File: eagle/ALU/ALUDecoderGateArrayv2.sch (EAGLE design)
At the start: 0 parts

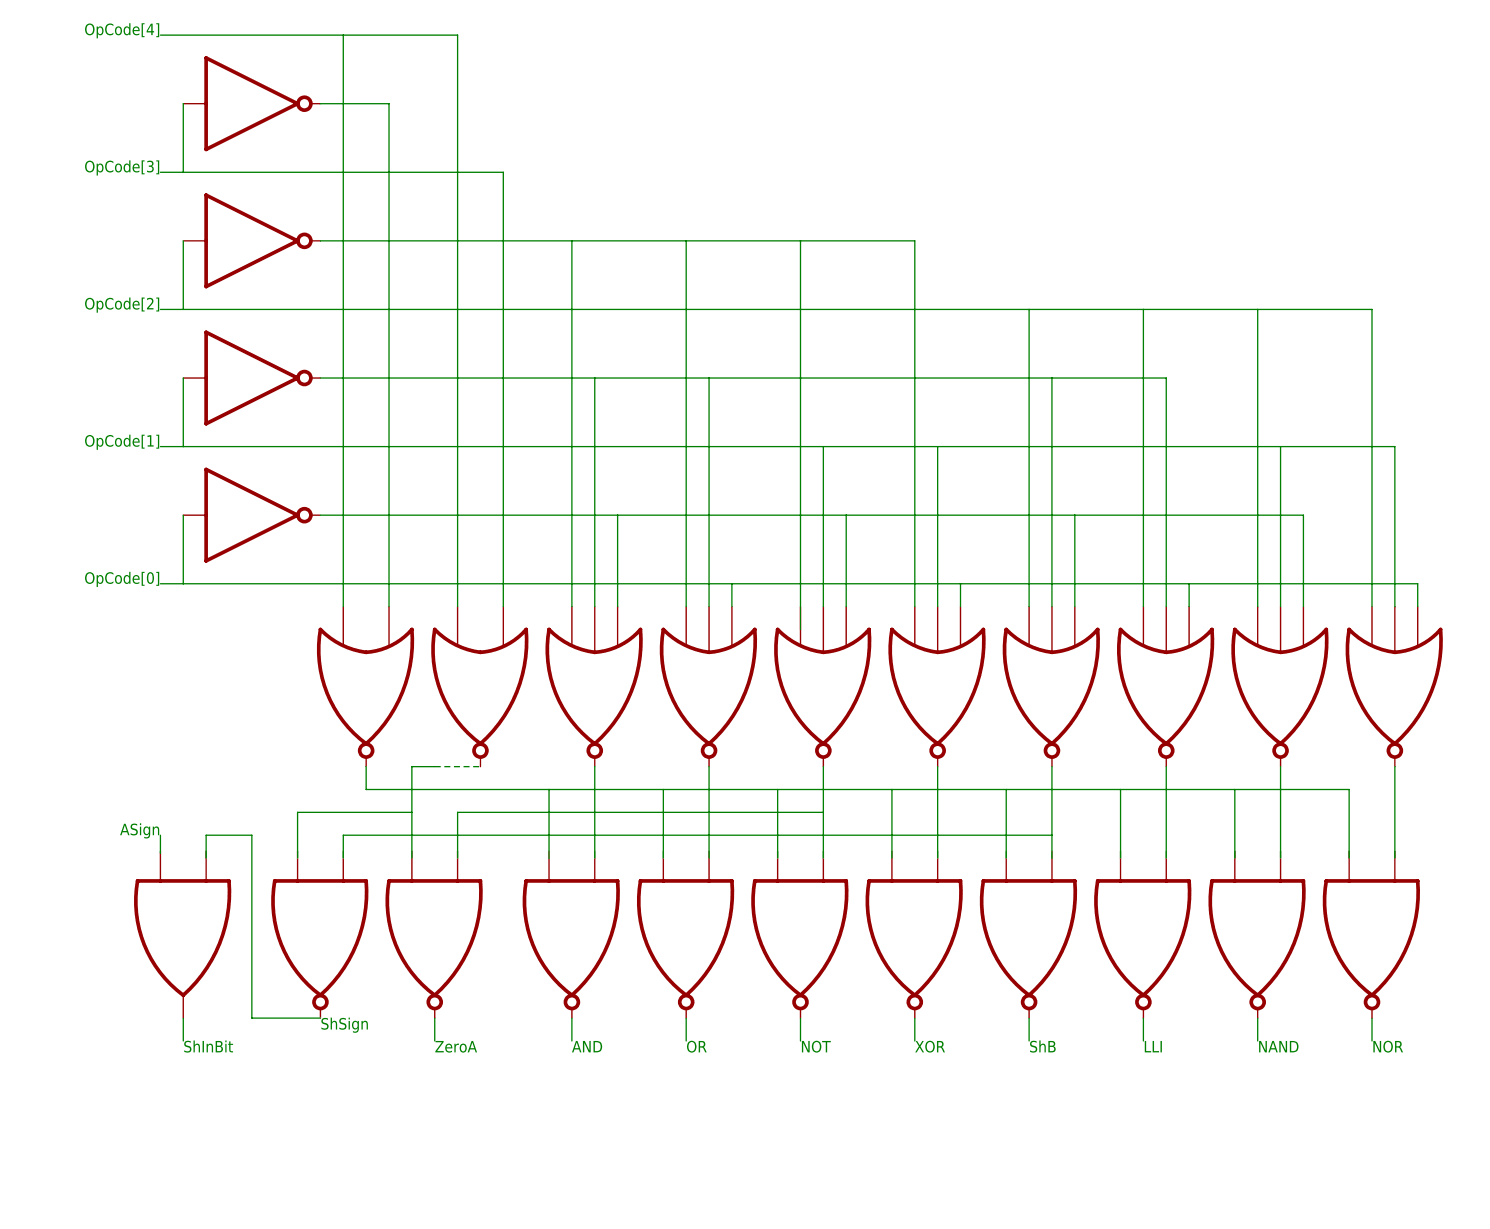
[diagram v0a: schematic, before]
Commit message: Eagle schematics now use library
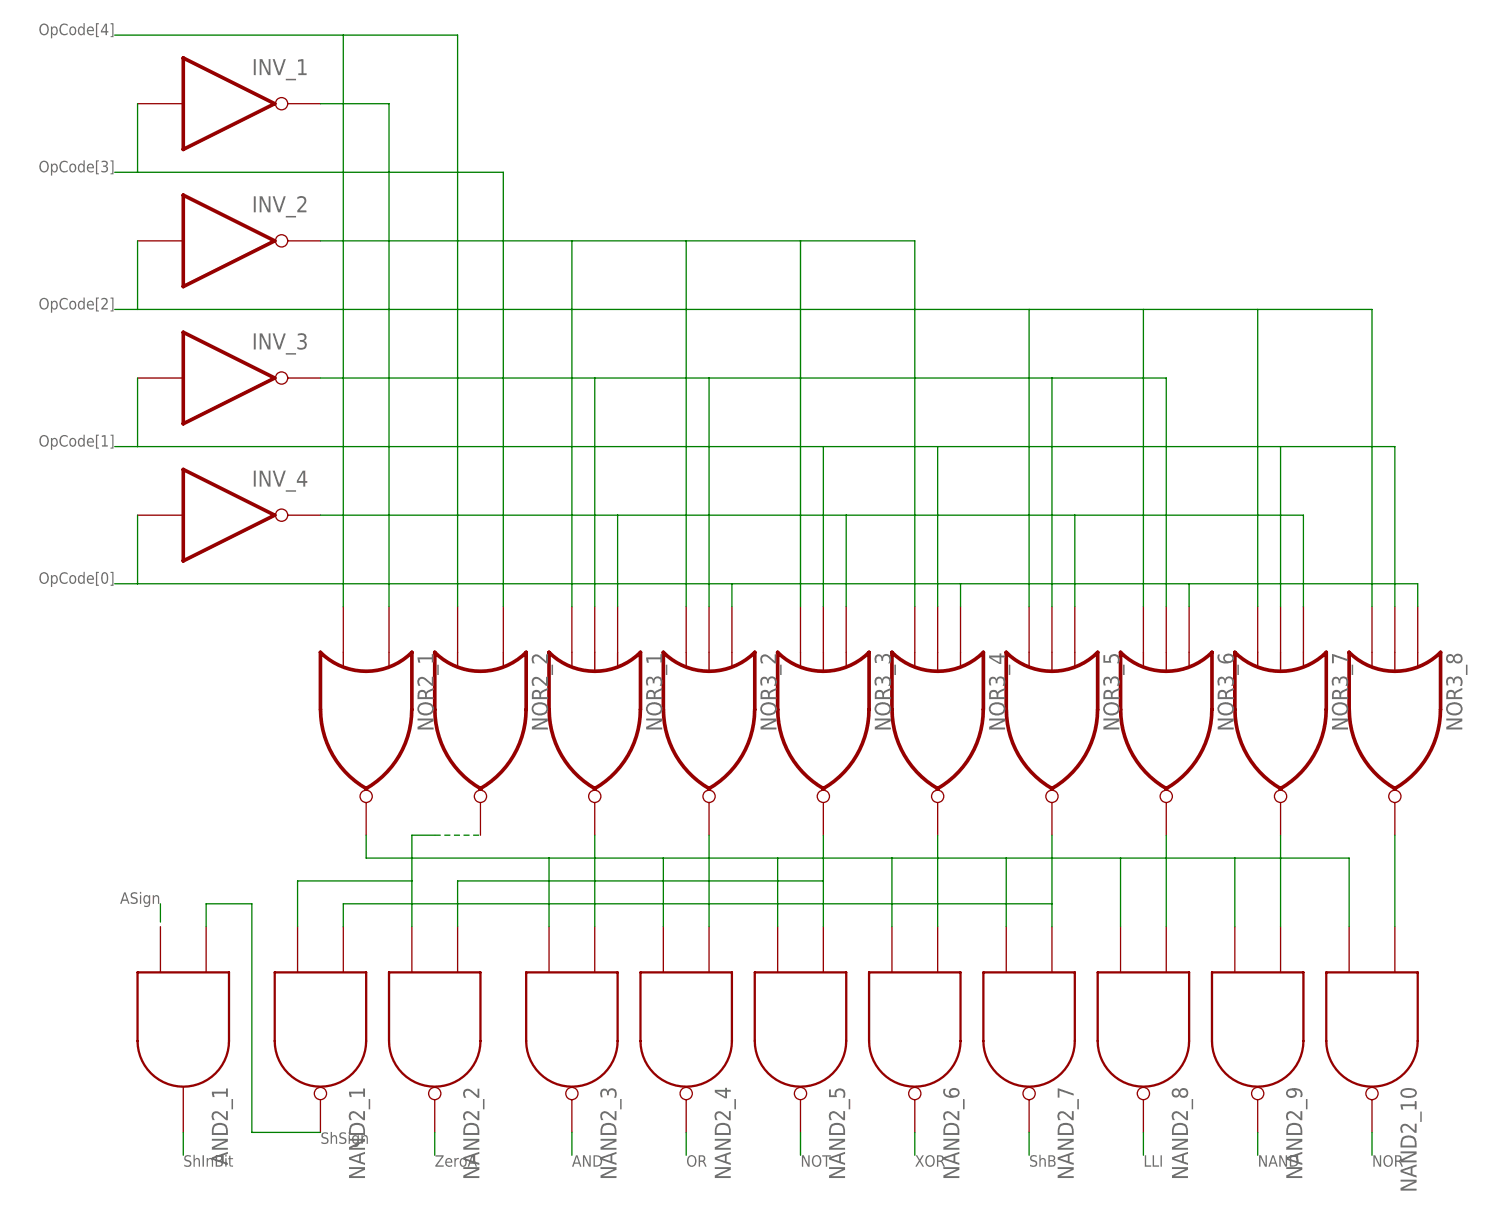
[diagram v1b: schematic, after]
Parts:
- added AND2_1: AND2, c035u:AND2
- added INV_1, INV_2, INV_3, INV_4: INV, c035u:INV
- added NAND2_1, NAND2_10, NAND2_2, NAND2_3, NAND2_4, NAND2_5, NAND2_6, NAND2_7, NAND2_8, NAND2_9: NAND2, c035u:NAND2
- added NOR2_1, NOR2_2: NOR2, c035u:NOR2
- added NOR3_1, NOR3_2, NOR3_3, NOR3_4, NOR3_5, NOR3_6, NOR3_7, NOR3_8: NOR3, c035u:NOR3
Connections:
- new net N$1: NOR2_1.I1, NOR2_2.I1
- new net N$10: INV_4.I, NOR3_2.I0, NOR3_4.I0, NOR3_6.I0, NOR3_8.I0
- new net N$11: INV_3.I, NOR3_3.I2, NOR3_4.I2, NOR3_7.I2, NOR3_8.I2
- new net N$12: NAND2_10.I1, NAND2_3.I1, NAND2_4.I1, NAND2_5.I1, NAND2_6.I1, NAND2_7.I1, NAND2_8.I1, NAND2_9.I1
- new net N$13: NAND2_2.A, NAND2_5.A
- new net N$14: NAND2_1.A, NAND2_7.A
- new net N$15: NAND2_10.A
- new net N$16: NAND2_3.A
- new net N$17: NAND2_4.A
- new net N$18: NAND2_6.A
- new net N$19: NAND2_8.A
- new net N$20: NAND2_9.A
- new net N$21: NAND2_2.O
- new net N$22: AND2_1.A, NAND2_1.O
- new net N$23: NAND2_1.I1, NAND2_2.I1
- new net N$24: NAND2_3.O
- new net N$25: NAND2_4.O
- new net N$26: NAND2_5.O
- new net N$27: NAND2_6.O
- new net N$28: NAND2_7.O
- new net N$29: NAND2_8.O
- new net N$3: INV_1.O, NOR2_1.I0
- new net N$30: NAND2_9.O
- new net N$31: NAND2_10.O
- new net N$4: NOR2_2.I0
- new net N$5: INV_2.I, NOR3_5.I1, NOR3_6.I1, NOR3_7.I1, NOR3_8.I1
- new net N$6: INV_2.O, NOR3_1.I1, NOR3_2.I1, NOR3_3.I1, NOR3_4.I1
- new net N$7: INV_3.O, NOR3_1.I2, NOR3_2.I2, NOR3_5.I2, NOR3_6.I2
- new net N$8: AND2_1.O
- new net N$9: INV_4.O, NOR3_1.I0, NOR3_3.I0, NOR3_5.I0, NOR3_7.I0

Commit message: Schematics small improvements
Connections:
- new net N$2: AND2_1.I1
- net N$12: now also NOR2_1.O
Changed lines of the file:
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@@
 <sheet>
 <plain>
-<text x="43.18" y="106.68" size="1.27" layer="95" rot="MR0">OpCode[4]</text>
-<text x="43.18" y="91.44" size="1.27" layer="95" rot="MR0">OpCode[3]</text>
-<text x="43.18" y="76.2" size="1.27" layer="95" rot="MR0">OpCode[2]</text>
-<text x="43.18" y="60.96" size="1.27" layer="95" rot="MR0">OpCode[1]</text>
-<text x="43.18" y="45.72" size="1.27" layer="95" rot="MR0">OpCode[0]</text>
-<text x="78.74" y="-17.78" size="1.27" layer="95" rot="MR180">ZeroA</text>
-<text x="66.04" y="-15.24" size="1.27" layer="95" rot="MR180">ShSign</text>
-<text x="93.98" y="-17.78" size="1.27" layer="95" rot="MR180">AND</text>
-<text x="106.68" y="-17.78" size="1.27" layer="95" rot="MR180">OR</text>
-<text x="119.38" y="-17.78" size="1.27" layer="95" rot="MR180">NOT</text>
-<text x="132.08" y="-17.78" size="1.27" layer="95" rot="MR180">XOR</text>
-<text x="170.18" y="-17.78" size="1.27" layer="95" rot="MR180">NAND</text>
-<text x="182.88" y="-17.78" size="1.27" layer="95" rot="MR180">NOR</text>
-<text x="157.48" y="-17.78" size="1.27" layer="95" rot="MR180">LLI</text>
-<text x="144.78" y="-17.78" size="1.27" layer="95" rot="MR180">ShB</text>
-<text x="48.26" y="10.16" size="1.27" layer="95" rot="MR0">ASign</text>
-<text x="50.8" y="-17.78" size="1.27" layer="95" rot="MR180">ShInBit</text>
+<text x="43.18" y="106.68" size="1.27" layer="91" rot="MR0">OpCode[4]</text>
+<text x="43.18" y="91.44" size="1.27" layer="91" rot="MR0">OpCode[3]</text>
+<text x="43.18" y="76.2" size="1.27" layer="91" rot="MR0">OpCode[2]</text>
+<text x="43.18" y="60.96" size="1.27" layer="91" rot="MR0">OpCode[1]</text>
+<text x="43.18" y="45.72" size="1.27" layer="91" rot="MR0">OpCode[0]</text>
+<text x="78.74" y="-17.78" size="1.27" layer="91" rot="MR180">ZeroA</text>
+<text x="66.04" y="-15.24" size="1.27" layer="91" rot="MR180">ShSign</text>
+<text x="93.98" y="-17.78" size="1.27" layer="91" rot="MR180">AND</text>
+<text x="106.68" y="-17.78" size="1.27" layer="91" rot="MR180">OR</text>
+<text x="119.38" y="-17.78" size="1.27" layer="91" rot="MR180">NOT</text>
+<text x="132.08" y="-17.78" size="1.27" layer="91" rot="MR180">XOR</text>
+<text x="170.18" y="-17.78" size="1.27" layer="91" rot="MR180">NAND</text>
+<text x="182.88" y="-17.78" size="1.27" layer="91" rot="MR180">NOR</text>
+<text x="157.48" y="-17.78" size="1.27" layer="91" rot="MR180">LLI</text>
+<text x="144.78" y="-17.78" size="1.27" layer="91" rot="MR180">ShB</text>
+<text x="48.26" y="10.16" size="1.27" layer="91" rot="MR0">ASign</text>
+<text x="50.8" y="-17.78" size="1.27" layer="91" rot="MR180">ShInBit</text>
 </plain>
 <instances>
@@
 <pinref part="NOR2_1" gate="G$1" pin="I1"/>
 <pinref part="NOR2_2" gate="G$1" pin="I1"/>
+<junction x="68.58" y="106.68"/>
 </segment>
 </net>
@@
 <wire x1="45.72" y1="91.44" x2="43.18" y2="91.44" width="0.1524" layer="91"/>
 <pinref part="NOR2_2" gate="G$1" pin="I0"/>
+<junction x="45.72" y="91.44"/>
 </segment>
 </net>
@@
 <pinref part="NOR3_7" gate="G$1" pin="I1"/>
 <pinref part="NOR3_8" gate="G$1" pin="I1"/>
+<junction x="45.72" y="76.2"/>
+<junction x="170.18" y="76.2"/>
+<junction x="157.48" y="76.2"/>
+<junction x="144.78" y="76.2"/>
 </segment>
 </net>
@@
 <pinref part="NOR3_3" gate="G$1" pin="I1"/>
 <pinref part="NOR3_4" gate="G$1" pin="I1"/>
+<junction x="93.98" y="83.82"/>
+<junction x="106.68" y="83.82"/>
+<junction x="119.38" y="83.82"/>
+<junction x="132.08" y="83.82"/>
 </segment>
 </net>
@@
 <pinref part="NOR3_5" gate="G$1" pin="I2"/>
 <pinref part="NOR3_6" gate="G$1" pin="I2"/>
+<junction x="96.52" y="68.58"/>
+<junction x="109.22" y="68.58"/>
+<junction x="147.32" y="68.58"/>
 </segment>
 </net>
@@
 <pinref part="NOR3_5" gate="G$1" pin="I0"/>
 <pinref part="NOR3_7" gate="G$1" pin="I0"/>
+<junction x="99.06" y="53.34"/>
+<junction x="124.46" y="53.34"/>
+<junction x="149.86" y="53.34"/>
 </segment>
 </net>
@@
 <pinref part="NOR3_6" gate="G$1" pin="I0"/>
 <pinref part="NOR3_8" gate="G$1" pin="I0"/>
+<junction x="45.72" y="45.72"/>
+<junction x="111.76" y="45.72"/>
+<junction x="137.16" y="45.72"/>
+<junction x="162.56" y="45.72"/>
 </segment>
 </net>
@@
 <pinref part="NOR3_7" gate="G$1" pin="I2"/>
 <pinref part="NOR3_8" gate="G$1" pin="I2"/>
+<junction x="45.72" y="60.96"/>
+<junction x="121.92" y="60.96"/>
+<junction x="134.62" y="60.96"/>
+<junction x="172.72" y="60.96"/>
 </segment>
 </net>
@@
 <pinref part="NAND2_9" gate="G$1" pin="I1"/>
 <pinref part="NAND2_10" gate="G$1" pin="I1"/>
+<pinref part="NOR2_1" gate="G$1" pin="O"/>
+<junction x="167.64" y="15.24"/>
+<junction x="154.94" y="15.24"/>
+<junction x="142.24" y="15.24"/>
+<junction x="129.54" y="15.24"/>
+<junction x="116.84" y="15.24"/>
+<junction x="104.14" y="15.24"/>
+<junction x="91.44" y="15.24"/>
 </segment>
 </net>
@@
 <pinref part="NAND2_2" gate="G$1" pin="A"/>
 <pinref part="NAND2_5" gate="G$1" pin="A"/>
+<junction x="121.92" y="12.7"/>
 </segment>
 </net>
@@
 <pinref part="NAND2_1" gate="G$1" pin="A"/>
 <pinref part="NAND2_7" gate="G$1" pin="A"/>
+<junction x="147.32" y="10.16"/>
 </segment>
 </net>
@@
 <segment>
 <wire x1="48.26" y1="10.16" x2="48.26" y2="8.128" width="0.1524" layer="91"/>
+<pinref part="AND2_1" gate="G$1" pin="I1"/>
+<wire x1="48.26" y1="7.62" x2="48.26" y2="8.128" width="0.1524" layer="91"/>
 </segment>
 </net>
@@
 <pinref part="NAND2_1" gate="G$1" pin="I1"/>
 <pinref part="NAND2_2" gate="G$1" pin="I1"/>
-</segment>
-</net>
+<junction x="76.2" y="12.7"/>
+</segment>
+</net>
